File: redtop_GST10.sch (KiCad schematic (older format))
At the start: 13 parts, among them J1 Conn_01x03, J2 Conn_01x05, U1 LMC6804, U2 4013

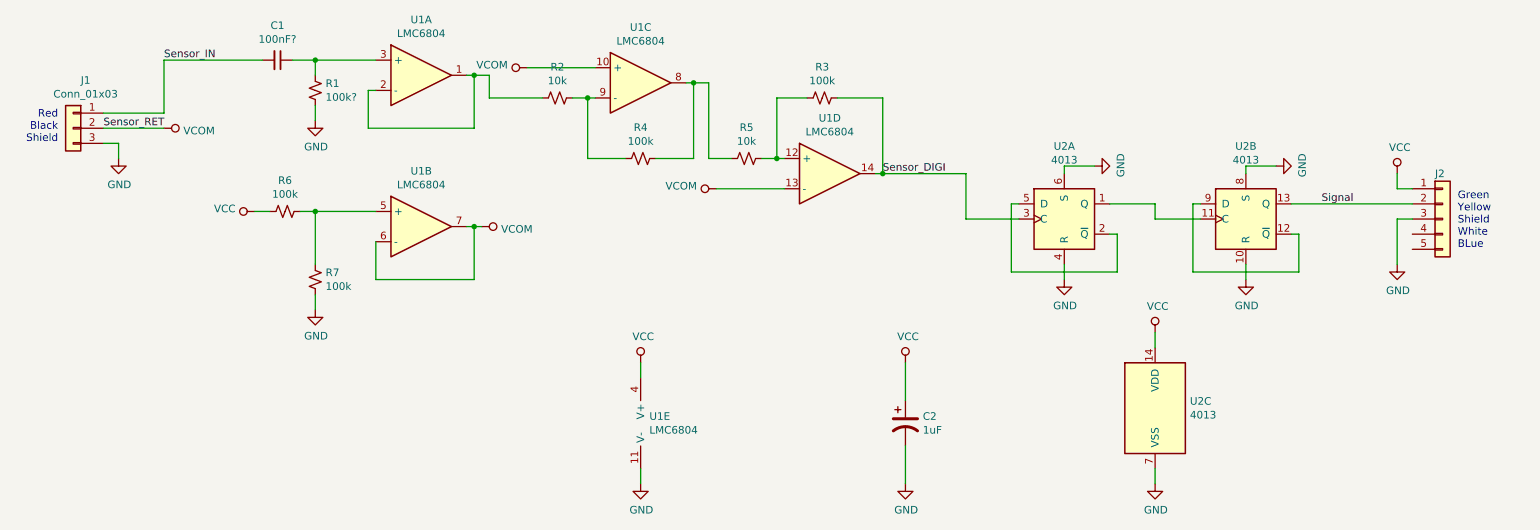
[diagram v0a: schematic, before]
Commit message: update schematic with correct components and Part numbers
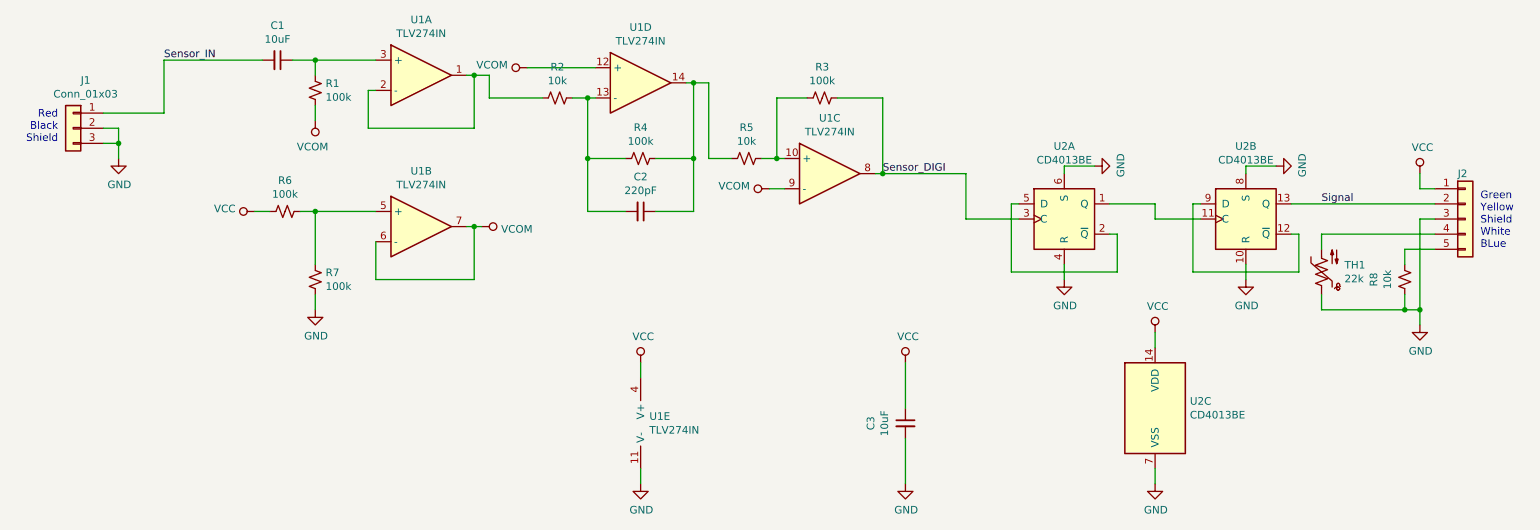
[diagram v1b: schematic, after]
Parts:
- removed C2: 1uF, Capacitor_THT:C_Radial_D6.3mm_H5.0mm_P2.50mm, symbol Device:CP1
- added C2: 220pF, Capacitor_THT:C_Disc_D4.3mm_W1.9mm_P5.00mm, symbol Device:C_Small
- added C3: 10uF, Capacitor_THT:C_Disc_D4.3mm_W1.9mm_P5.00mm, symbol Device:C_Small
- added R8: 10k, Resistor_THT:R_Axial_DIN0207_L6.3mm_D2.5mm_P7.62mm_Horizontal, symbol Device:R_Small_US
- added TH1: 22k, Resistor_THT:R_Axial_DIN0204_L3.6mm_D1.6mm_P2.54mm_Vertical, symbol Device:Thermistor_NTC_US
- C1: value 100nF? -> 10uF; footprint Capacitor_THT:C_Disc_D4.7mm_W2.5mm_P5.00mm -> Capacitor_THT:C_Disc_D4.3mm_W1.9mm_P5.00mm; Supplier (none) -> Digi-Key; Supplier Part Number (none) -> 445-181284-1-ND
- J1, J2: Supplier (none) -> OMIT; Supplier Part Number (none) -> NOSTUFF
- R1: value 100k? -> 100k; Supplier (none) -> Digi-Key; Supplier Part Number (none) -> CF14JT100KCT-ND
- R2, R5: Supplier (none) -> Digi-Key; Supplier Part Number (none) -> CF14JT10K0CT-ND
- R3, R4, R6, R7: Supplier (none) -> Digi-Key; Supplier Part Number (none) -> CF14JT100KCT-ND
- U1: value LMC6804 -> TLV274IN; Supplier (none) -> Digi-Key; Supplier Part Number (none) -> 296-14379-5-ND
- U2: value 4013 -> CD4013BE; Supplier (none) -> Digi-Key; Supplier Part Number (none) -> 296-2033-5-ND
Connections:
- net GND: now also J1.2 (Pin_2), C3.2, R8.1, TH1.1; no longer R1.2
- net Sensor_DIGI: now also U1.8; no longer U1.14
- net VCC: now also C3.1
- net VCOM: now also R1.2, U1.12 (+), U1.9 (-); no longer J1.2 (Pin_2), U1.10 (+), U1.13 (-)
- net at R3.1, R5.2: now also U1.10 (+); no longer U1.12 (+)
- net at R4.2, R5.1: now also U1.14, C2.1; no longer U1.8
- net at R2.2, R4.1: now also U1.13 (-), C2.2; no longer U1.9 (-)
- net at J2.4 (Pin_4): now also TH1.2
- net at J2.5 (Pin_5): now also R8.2
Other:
- moved on the sheet: J2, U1C, U1D

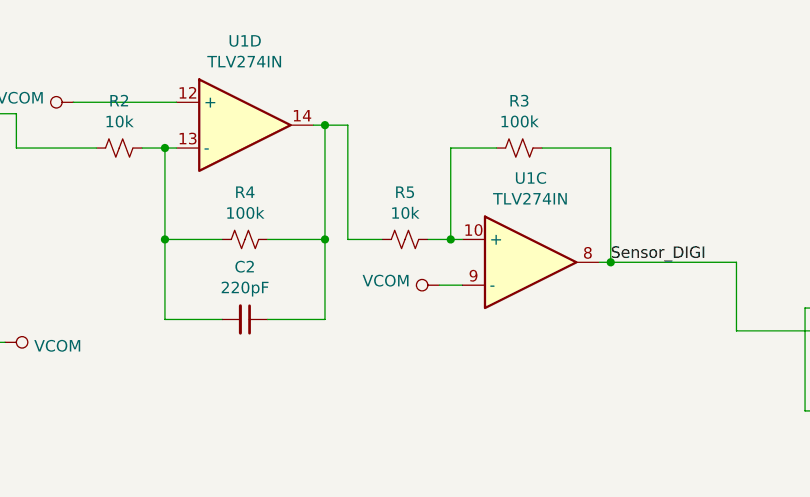
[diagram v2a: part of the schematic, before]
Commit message: update hysteresis resistor to as-built
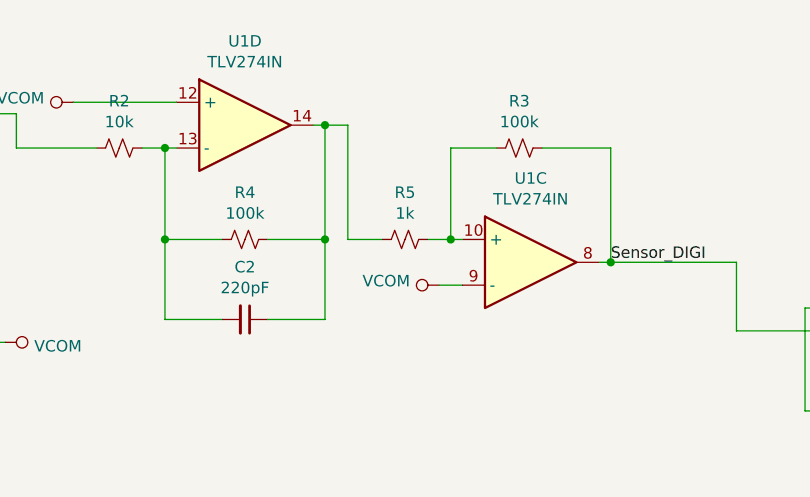
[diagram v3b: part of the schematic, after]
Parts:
- R5: value 10k -> 1k; Supplier Part Number CF14JT10K0CT-ND -> CF14JT1K00CT-ND
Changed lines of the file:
@@
 P 5850 3200
 F 0 "R5" V 6055 3200 50  0000 C CNN
-F 1 "10k" V 5964 3200 50  0000 C CNN
+F 1 "1k" V 5964 3200 50  0000 C CNN
 F 2 "Resistor_THT:R_Axial_DIN0207_L6.3mm_D2.5mm_P7.62mm_Horizontal" H 5850 3200 50  0001 C CNN
 F 3 "https://www.seielect.com/catalog/sei-cf_cfm.pdf" H 5850 3200 50  0001 C CNN
 F 4 "Digi-Key" H 5850 3200 50  0001 C CNN "Supplier"
-F 5 "CF14JT10K0CT-ND" H 5850 3200 50  0001 C CNN "Supplier Part Number"
+F 5 "CF14JT1K00CT-ND" H 5850 3200 50  0001 C CNN "Supplier Part Number"
 	1    5850 3200
 	0    -1   -1   0
